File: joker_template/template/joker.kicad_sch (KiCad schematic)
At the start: 22 parts, among them J1 SM04B-SRSS-TB(LF)(SN), U1 BL24C256A-SFRC, U2 STM32F411CEU6, X1 ARM JTAG, X2 EXTRA PINS, Y1 7325-0800A2010-00

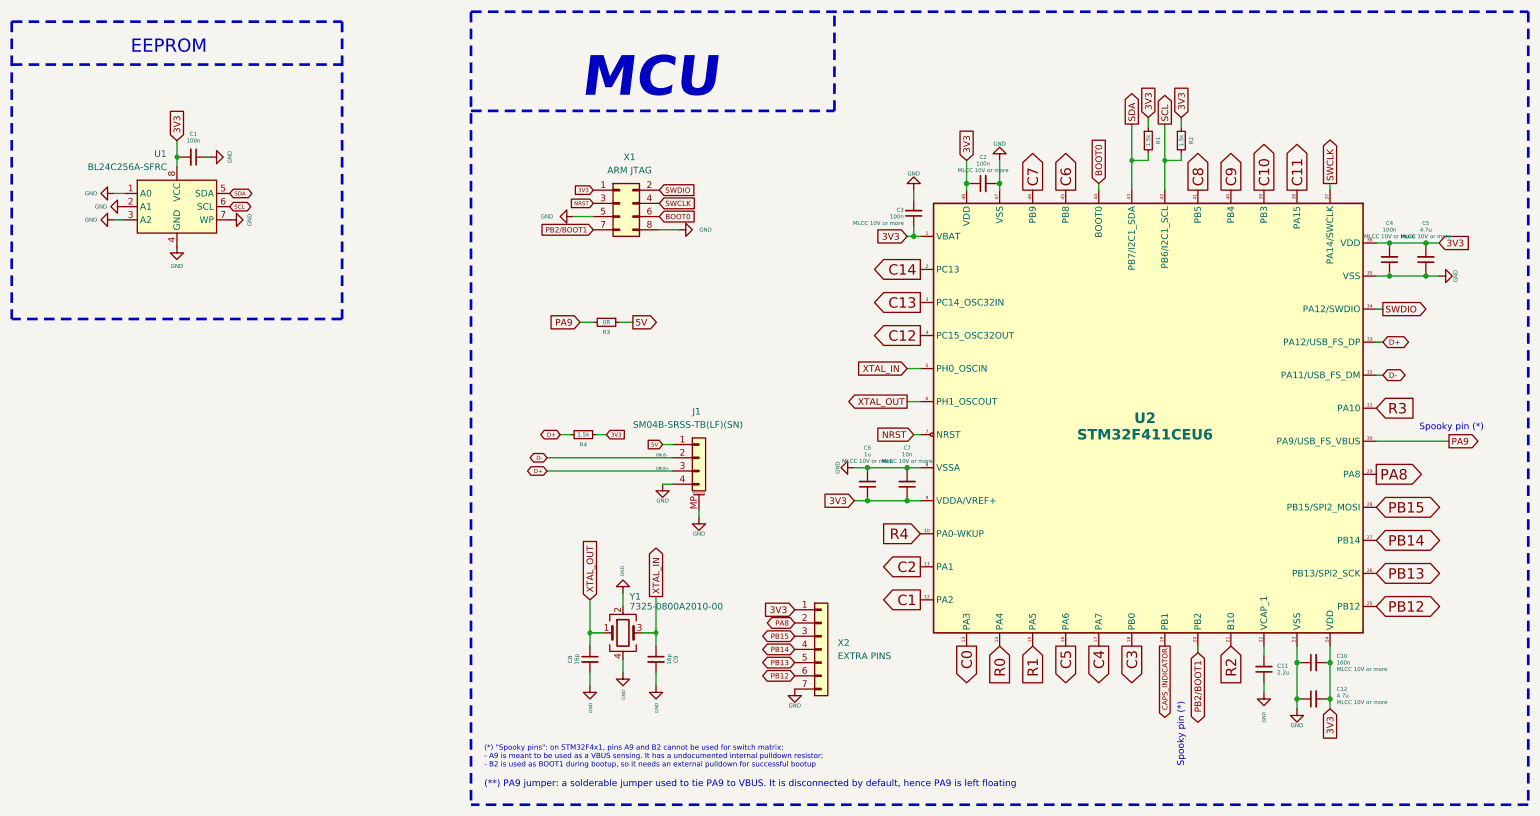
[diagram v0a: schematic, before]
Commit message: New makefile version for joker template
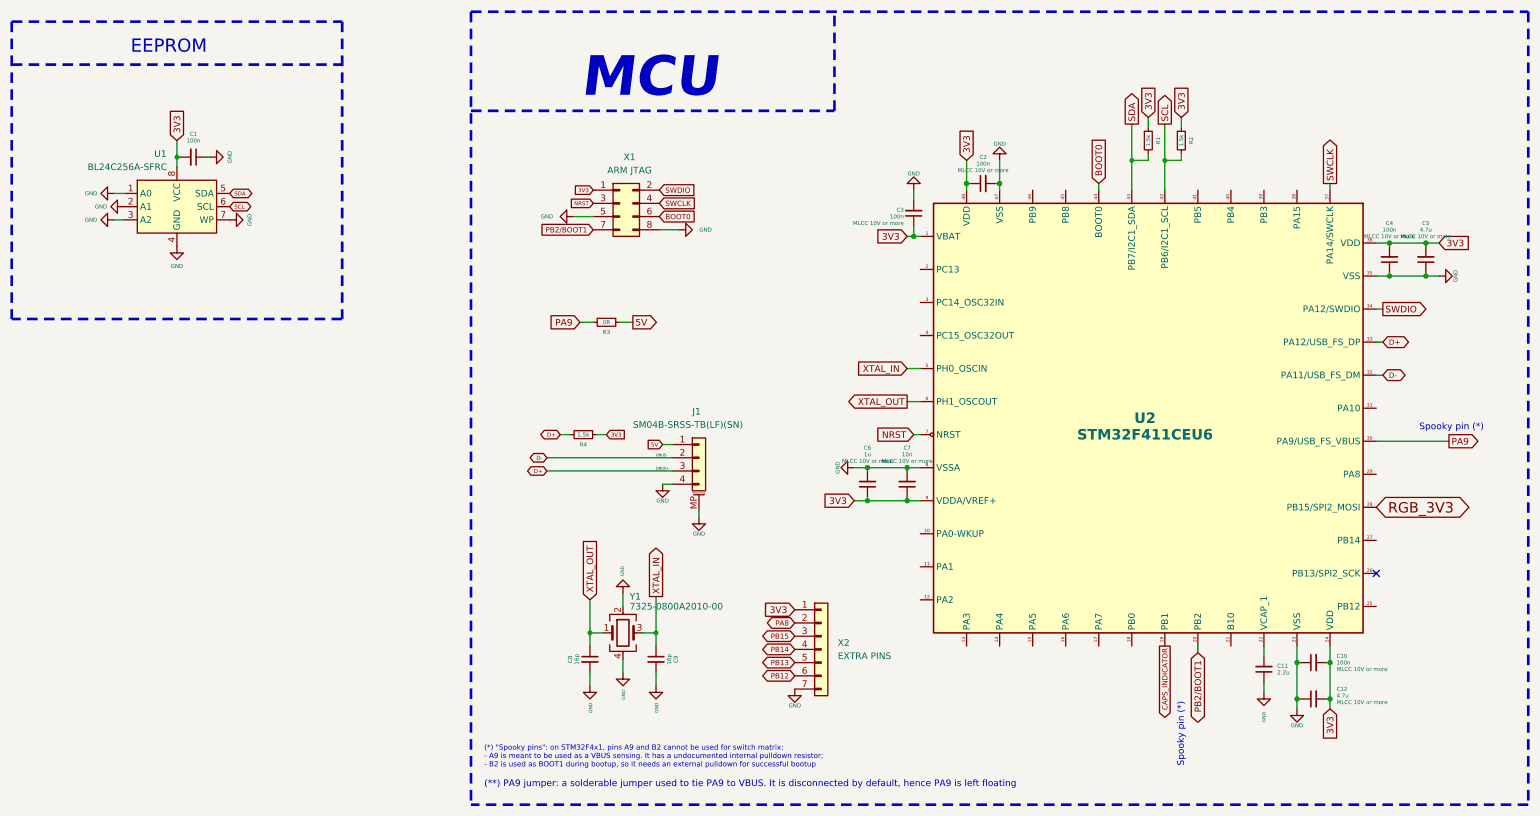
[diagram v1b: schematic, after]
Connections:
- net PA8: no longer U2.29 (PA8)
- net PB12: no longer U2.25 (PB12)
- net PB13: no longer U2.26 (PB13)
- net PB14: no longer U2.27 (PB14)
- net PB15: no longer U2.28 (PB15)
- net C0: no longer names the net of U2.13 (PA3)
- net C1: no longer names the net of U2.12 (PA2)
- net C10: no longer names the net of U2.39 (PB3)
- net C11: no longer names the net of U2.38 (PA15)
- net C12: no longer names the net of U2.4 (PC15_OSC32OUT)
- net C13: no longer names the net of U2.3 (PC14_OSC32IN)
- net C14: no longer names the net of U2.2 (PC13)
- net C2: no longer names the net of U2.11 (PA1)
- net C3: no longer names the net of U2.18 (PB0)
- net C4: no longer names the net of U2.17 (PA7)
- net C5: no longer names the net of U2.16 (PA6)
- net C6: no longer names the net of U2.45 (PB8)
- net C7: no longer names the net of U2.46 (PB9)
- net C8: no longer names the net of U2.41 (PB5)
- net C9: no longer names the net of U2.40 (PB4)
- net R0: no longer names the net of U2.14 (PA4)
- net R1: no longer names the net of U2.15 (PA5)
- net R2: no longer names the net of U2.21 (B10)
- net R3: no longer names the net of U2.31 (PA10)
- net R4: no longer names the net of U2.10 (PA0-WKUP)
- new net RGB_3V3: U2.28 (PB15)
- no-connect marks 0 -> 1
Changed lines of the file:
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@@
   (junction (at 298.45 62.23) (diameter 1.016) (color 0 0 0 0))
   (junction (at 298.45 68.58) (diameter 1.016) (color 0 0 0 0))
+  (no_connect (at 288.925 125.73))
   (wire (pts (xy 46.355 52.705) (xy 48.26 52.705))
     (stroke (width 0) (type solid) (color 0 0 0 0))
@@
     )
   )
-  (global_label "C14" (shape output) (at 201.295 67.31 180) (fields_autoplaced)
-    (effects (font (size 2 2)) (justify right))
-    (property "Intersheet References" "${INTERSHEET_REFS}" (id 0) (at 191.6855 67.435 0)
-      (effects (font (size 2 2)) (justify right) hide)
-    )
-  )
-  (global_label "C13" (shape output) (at 201.295 73.66 180) (fields_autoplaced)
-    (effects (font (size 2 2)) (justify right))
-    (property "Intersheet References" "${INTERSHEET_REFS}" (id 0) (at 191.6855 73.785 0)
-      (effects (font (size 2 2)) (justify right) hide)
-    )
-  )
-  (global_label "C12" (shape output) (at 201.295 80.01 180) (fields_autoplaced)
-    (effects (font (size 2 2)) (justify right))
-    (property "Intersheet References" "${INTERSHEET_REFS}" (id 0) (at 191.6855 80.135 0)
-      (effects (font (size 2 2)) (justify right) hide)
-    )
-  )
-  (global_label "R4" (shape input) (at 201.295 118.11 180) (fields_autoplaced)
-    (effects (font (size 2 2)) (justify right))
-    (property "Intersheet References" "${INTERSHEET_REFS}" (id 0) (at 193.5902 117.985 0)
-      (effects (font (size 2 2)) (justify right) hide)
-    )
-  )
-  (global_label "C2" (shape output) (at 201.295 124.46 180) (fields_autoplaced)
-    (effects (font (size 2 2)) (justify right))
-    (property "Intersheet References" "${INTERSHEET_REFS}" (id 0) (at 193.5902 124.335 0)
-      (effects (font (size 2 2)) (justify right) hide)
-    )
-  )
-  (global_label "C1" (shape output) (at 201.295 130.81 180) (fields_autoplaced)
-    (effects (font (size 2 2)) (justify right))
-    (property "Intersheet References" "${INTERSHEET_REFS}" (id 0) (at 193.5902 130.685 0)
-      (effects (font (size 2 2)) (justify right) hide)
-    )
-  )
   (global_label "3V3" (shape input) (at 210.185 46.355 90)
     (effects (font (size 1.27 1.27)) (justify left))
@@
     )
   )
-  (global_label "C0" (shape output) (at 210.185 139.7 270) (fields_autoplaced)
-    (effects (font (size 2 2)) (justify right))
-    (property "Intersheet References" "${INTERSHEET_REFS}" (id 0) (at 210.06 147.4048 90)
-      (effects (font (size 2 2)) (justify right) hide)
-    )
-  )
-  (global_label "R0" (shape input) (at 216.535 139.7 270) (fields_autoplaced)
-    (effects (font (size 2 2)) (justify right))
-    (property "Intersheet References" "${INTERSHEET_REFS}" (id 0) (at 216.41 147.4048 90)
-      (effects (font (size 2 2)) (justify right) hide)
-    )
-  )
-  (global_label "C7" (shape output) (at 222.885 52.07 90) (fields_autoplaced)
-    (effects (font (size 2 2)) (justify left))
-    (property "Intersheet References" "${INTERSHEET_REFS}" (id 0) (at 222.76 44.3652 90)
-      (effects (font (size 2 2)) (justify left) hide)
-    )
-  )
-  (global_label "R1" (shape input) (at 222.885 139.7 270) (fields_autoplaced)
-    (effects (font (size 2 2)) (justify right))
-    (property "Intersheet References" "${INTERSHEET_REFS}" (id 0) (at 222.76 147.4048 90)
-      (effects (font (size 2 2)) (justify right) hide)
-    )
-  )
-  (global_label "C6" (shape output) (at 229.235 52.07 90) (fields_autoplaced)
-    (effects (font (size 2 2)) (justify left))
-    (property "Intersheet References" "${INTERSHEET_REFS}" (id 0) (at 229.11 44.3652 90)
-      (effects (font (size 2 2)) (justify left) hide)
-    )
-  )
-  (global_label "C5" (shape output) (at 229.235 139.7 270) (fields_autoplaced)
-    (effects (font (size 2 2)) (justify right))
-    (property "Intersheet References" "${INTERSHEET_REFS}" (id 0) (at 229.11 147.4048 90)
-      (effects (font (size 2 2)) (justify right) hide)
-    )
-  )
   (global_label "BOOT0" (shape input) (at 235.585 50.8 90)
     (effects (font (size 1.27 1.27)) (justify left))
     (property "Intersheet References" "${INTERSHEET_REFS}" (id 0) (at -439.42 -7.62 0)
       (effects (font (size 1.27 1.27)) hide)
-    )
-  )
-  (global_label "C4" (shape output) (at 235.585 139.7 270) (fields_autoplaced)
-    (effects (font (size 2 2)) (justify right))
-    (property "Intersheet References" "${INTERSHEET_REFS}" (id 0) (at 235.46 147.4048 90)
-      (effects (font (size 2 2)) (justify right) hide)
     )
   )
@@
     (property "Intersheet References" "${INTERSHEET_REFS}" (id 0) (at 241.8556 33.3888 90)
       (effects (font (size 1.27 1.27)) (justify left) hide)
-    )
-  )
-  (global_label "C3" (shape output) (at 241.935 139.7 270) (fields_autoplaced)
-    (effects (font (size 2 2)) (justify right))
-    (property "Intersheet References" "${INTERSHEET_REFS}" (id 0) (at 241.81 147.4048 90)
-      (effects (font (size 2 2)) (justify right) hide)
     )
   )
@@
     )
   )
-  (global_label "C8" (shape output) (at 254.635 52.07 90) (fields_autoplaced)
-    (effects (font (size 2 2)) (justify left))
-    (property "Intersheet References" "${INTERSHEET_REFS}" (id 0) (at 254.51 44.3652 90)
-      (effects (font (size 2 2)) (justify left) hide)
-    )
-  )
   (global_label "PB2{slash}BOOT1" (shape bidirectional) (at 254.635 140.97 270)
     (effects (font (size 1.27 1.27)) (justify right))
@@
     )
   )
-  (global_label "C9" (shape output) (at 260.985 52.07 90) (fields_autoplaced)
+  (global_label "SWCLK" (shape output) (at 280.035 50.8 90)
+    (effects (font (size 1.27 1.27)) (justify left))
+    (property "Intersheet References" "${INTERSHEET_REFS}" (id 0) (at -439.42 -7.62 0)
+      (effects (font (size 1.27 1.27)) hide)
+    )
+  )
+  (global_label "3V3" (shape input) (at 280.035 151.765 270)
+    (effects (font (size 1.27 1.27)) (justify right))
+    (property "Intersheet References" "${INTERSHEET_REFS}" (id 0) (at -439.42 -7.62 0)
+      (effects (font (size 1.27 1.27)) hide)
+    )
+  )
+  (global_label "RGB_3V3" (shape bidirectional) (at 288.925 113.03 0) (fields_autoplaced)
     (effects (font (size 2 2)) (justify left))
-    (property "Intersheet References" "${INTERSHEET_REFS}" (id 0) (at 260.86 44.3652 90)
+    (property "Intersheet References" "${INTERSHEET_REFS}" (id 0) (at 305.7726 112.905 0)
       (effects (font (size 2 2)) (justify left) hide)
     )
-  )
-  (global_label "R2" (shape input) (at 260.985 139.7 270) (fields_autoplaced)
-    (effects (font (size 2 2)) (justify right))
-    (property "Intersheet References" "${INTERSHEET_REFS}" (id 0) (at 260.86 147.4048 90)
-      (effects (font (size 2 2)) (justify right) hide)
-    )
-  )
-  (global_label "C10" (shape output) (at 267.335 52.07 90) (fields_autoplaced)
-    (effects (font (size 2 2)) (justify left))
-    (property "Intersheet References" "${INTERSHEET_REFS}" (id 0) (at 267.21 42.4605 90)
-      (effects (font (size 2 2)) (justify left) hide)
-    )
-  )
-  (global_label "C11" (shape output) (at 273.685 52.07 90) (fields_autoplaced)
-    (effects (font (size 2 2)) (justify left))
-    (property "Intersheet References" "${INTERSHEET_REFS}" (id 0) (at 273.56 42.4605 90)
-      (effects (font (size 2 2)) (justify left) hide)
-    )
-  )
-  (global_label "SWCLK" (shape output) (at 280.035 50.8 90)
-    (effects (font (size 1.27 1.27)) (justify left))
-    (property "Intersheet References" "${INTERSHEET_REFS}" (id 0) (at -439.42 -7.62 0)
-      (effects (font (size 1.27 1.27)) hide)
-    )
-  )
-  (global_label "3V3" (shape input) (at 280.035 151.765 270)
-    (effects (font (size 1.27 1.27)) (justify right))
-    (property "Intersheet References" "${INTERSHEET_REFS}" (id 0) (at -439.42 -7.62 0)
-      (effects (font (size 1.27 1.27)) hide)
-    )
-  )
-  (global_label "R3" (shape input) (at 288.925 93.98 0) (fields_autoplaced)
-    (effects (font (size 2 2)) (justify left))
-    (property "Intersheet References" "${INTERSHEET_REFS}" (id 0) (at 296.6298 93.855 0)
-      (effects (font (size 2 2)) (justify left) hide)
-    )
-  )
-  (global_label "PA8" (shape output) (at 288.925 106.68 0) (fields_autoplaced)
-    (effects (font (size 2 2)) (justify left))
-    (property "Intersheet References" "${INTERSHEET_REFS}" (id 0) (at 298.344 106.555 0)
-      (effects (font (size 2 2)) (justify left) hide)
-    )
-  )
-  (global_label "PB15" (shape bidirectional) (at 288.925 113.03 0) (fields_autoplaced)
-    (effects (font (size 2 2)) (justify left))
-    (property "Intersheet References" "${INTERSHEET_REFS}" (id 0) (at 300.5345 112.905 0)
-      (effects (font (size 2 2)) (justify left) hide)
-    )
-  )
-  (global_label "PB14" (shape bidirectional) (at 288.925 119.38 0) (fields_autoplaced)
-    (effects (font (size 2 2)) (justify left))
-    (property "Intersheet References" "${INTERSHEET_REFS}" (id 0) (at 300.5345 119.255 0)
-      (effects (font (size 2 2)) (justify left) hide)
-    )
-  )
-  (global_label "PB13" (shape bidirectional) (at 288.925 125.73 0) (fields_autoplaced)
-    (effects (font (size 2 2)) (justify left))
-    (property "Intersheet References" "${INTERSHEET_REFS}" (id 0) (at 300.5345 125.605 0)
-      (effects (font (size 2 2)) (justify left) hide)
-    )
-  )
-  (global_label "PB12" (shape bidirectional) (at 288.925 132.08 0) (fields_autoplaced)
-    (effects (font (size 2 2)) (justify left))
-    (property "Intersheet References" "${INTERSHEET_REFS}" (id 0) (at 300.5345 131.955 0)
-      (effects (font (size 2 2)) (justify left) hide)
-    )

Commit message: New version of joker template
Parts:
- removed J1: SM04B-SRSS-TB(LF)(SN), acheron_Connectors:SM04B-SRSS-TB(LF)(SN)_mounting-reliefs, symbol Connector_Generic_MountingPin:Conn_01x04_MountingPin
- removed X2: EXTRA PINS, acheron_Connectors:PinHeader_1x7_P2.54mm_Vertical, symbol Connector_Generic:Conn_01x07
- U2: footprint acheron_Components:STM_UFQFPN-48_LQFP-48-1EP_7x7mm_P0.5mm_HandSoldering -> acheron_Components:STM_UFQFPN-48_LQFP-48-1EP_7x7mm_P0.5mm_HandSoldering_ThermalReliefs
- X1: footprint acheron_Connectors:PinHeader_2x4_P2.54mm_Vertical_Staggered -> acheron_Connectors:PinHeader_2x5_P2.54mm_Vertical_Staggered; symbol Connector_Generic:Conn_02x04_Odd_Even -> Connector_Generic:Conn_02x05_Odd_Even
- Y1: Manufacturer Part Number (none) -> 7325-0800A2010-00
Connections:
- net 3V3: now also X1.7 (Pin_7), X1.8 (Pin_8); no longer X1.1 (Pin_1)
- net BOOT0: now also X1.5 (Pin_5); no longer X1.6 (Pin_6)
- net GND: now also X1.10 (Pin_10), X1.3 (Pin_3), X1.4 (Pin_4); no longer X1.5 (Pin_5), X1.8 (Pin_8)
- net NRST: now also X1.9 (Pin_9); no longer X1.3 (Pin_3)
- net PB2/BOOT1: now also X1.6 (Pin_6); no longer X1.7 (Pin_7)
- net SWCLK: now also X1.2 (Pin_2); no longer X1.4 (Pin_4)
- net SWDIO: now also X1.1 (Pin_1); no longer X1.2 (Pin_2)
- net LED_PWM: now reaches U2.16 (PA6)
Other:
- moved on the sheet: R3, R4
